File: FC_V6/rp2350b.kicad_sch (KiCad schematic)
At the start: 44 parts, among them J1 USB_C_Receptacle_USB2.0_16P, J2 Conn_ARM_JTAG_SWD_10, SW1 KMR2, SW2 KMR2, U1 RP2350B, U2 W25Q128JV, Y1 ABM8-272-T3

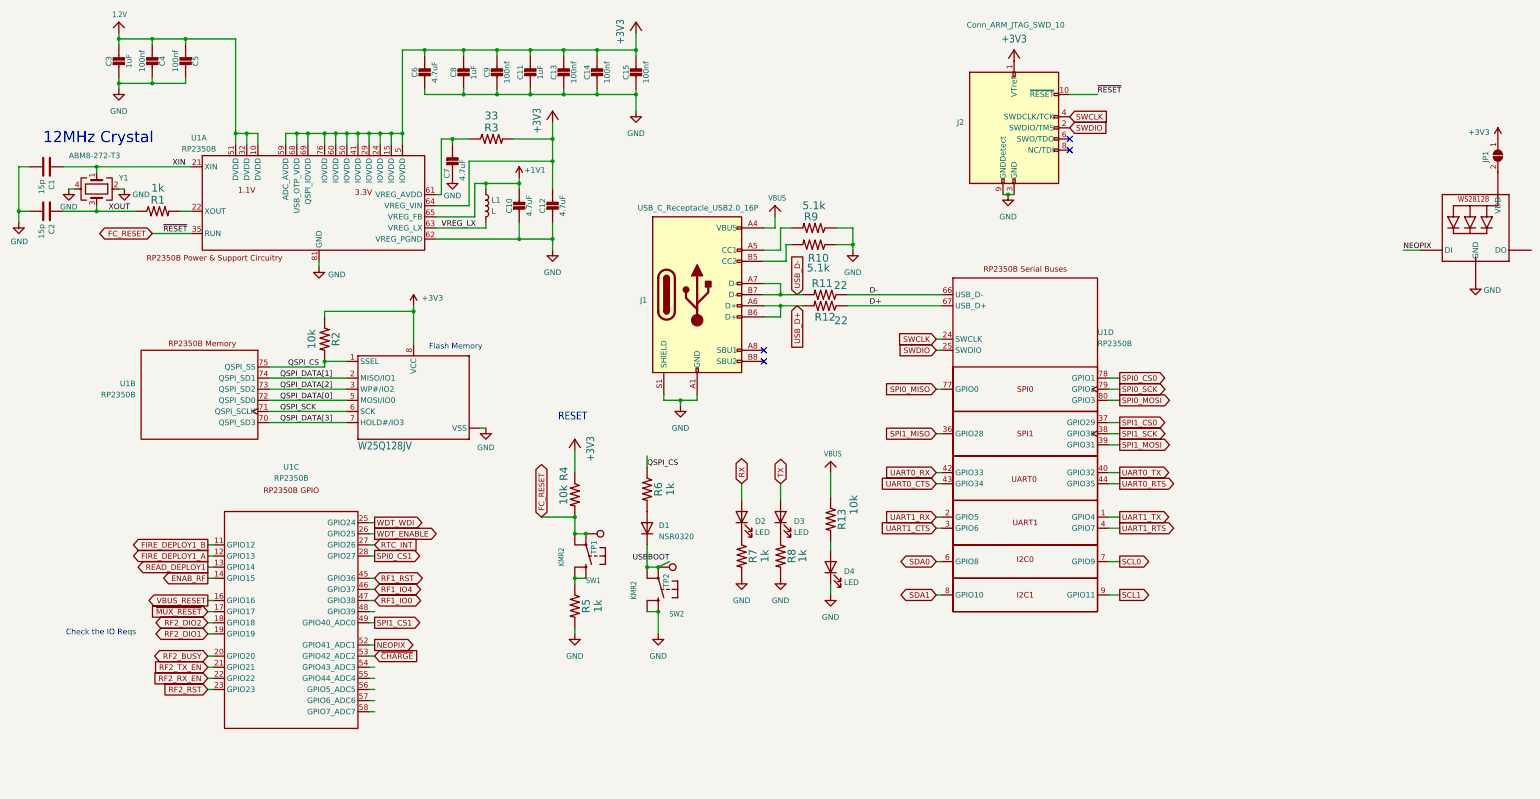
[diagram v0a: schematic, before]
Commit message: Updated Flash Memory Schematic
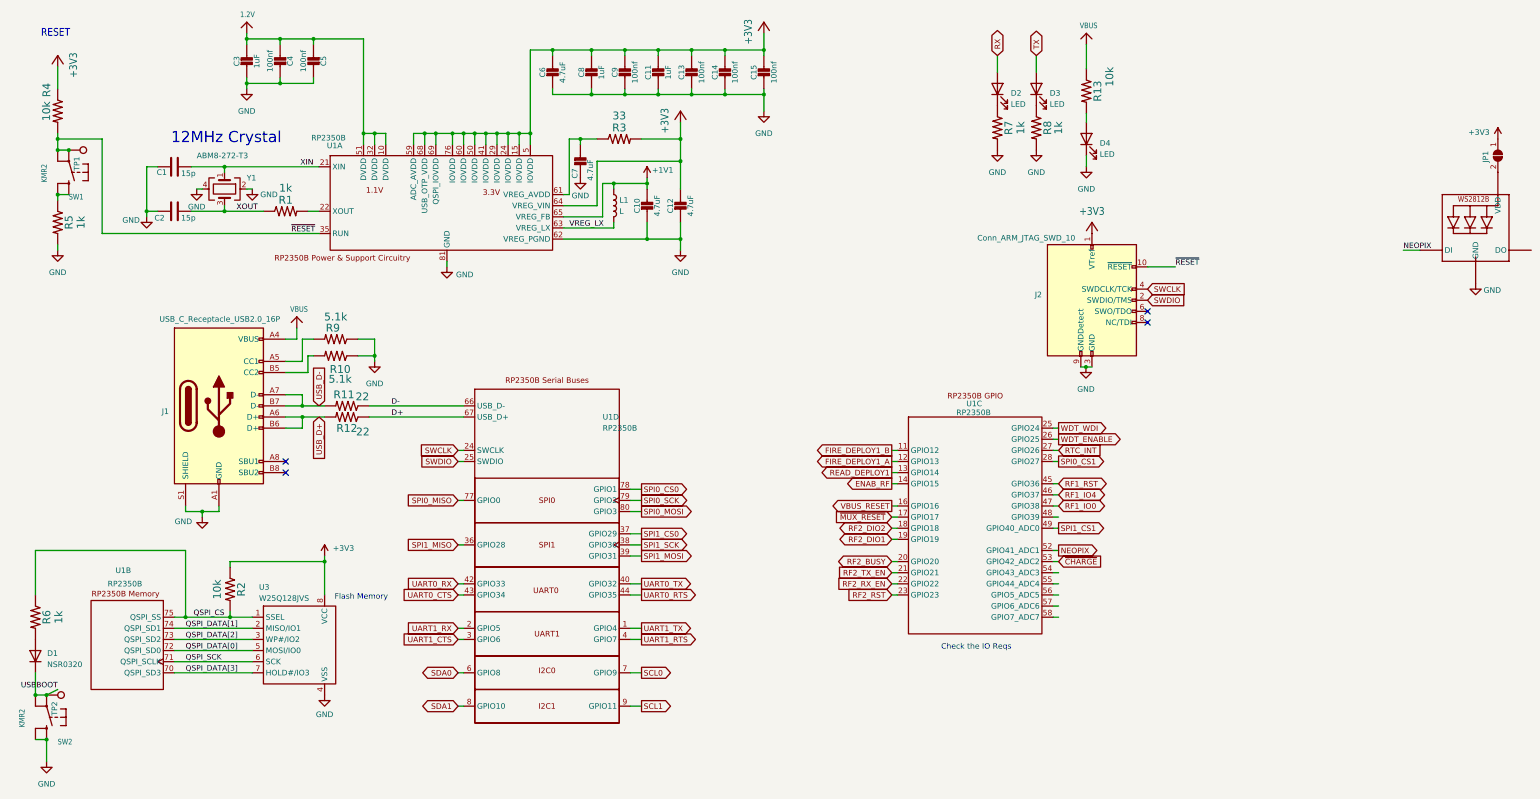
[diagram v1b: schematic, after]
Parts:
- removed U2: W25Q128JV, Package_SO:SOIC-8_5.275x5.275mm_P1.27mm, symbol Adafruit ItsyBitsy RP2040-eagle-import:SPIFLASH_8PIN_4X4
- added U3: W25Q128JVS, Package_SO:SOIC-8_5.3x5.3mm_P1.27mm, symbol PROVES:W25Q128JV
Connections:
- net +3V3: now also U3.8 (VCC)
- net GND: now also U3.4 (VSS)
- net QSPI_CS: now also U3.1 (SSEL)
- net QSPI_DATA[0]: now also U3.5 (MOSI/IO0)
- net QSPI_DATA[1]: now also U3.2 (MISO/IO1)
- net QSPI_DATA[2]: now also U3.3 (WP#/IO2)
- net QSPI_DATA[3]: now also U3.7 (HOLD#/IO3)
- net QSPI_SCK: now also U3.6 (SCK)
- net FC_RESET renamed ~{RESET}
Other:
- moved on the sheet: C1, C10, C11, C12, C13, C14, C15, C2, C3, C4, C5, C6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

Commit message: Updated LSM6DSOX Symbol
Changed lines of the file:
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@@
 		(on_board yes)
 		(dnp no)
-		(fields_autoplaced yes)
 		(property "Reference" "U1"
-			(at 149.86 109.2171 0)
+			(at 152.146 98.298 0)
 			(effects
 				(font
@@
 		)
 		(property "Value" "RP2350B"
-			(at 149.86 111.7571 0)
+			(at 152.146 100.838 0)
 			(effects
 				(font

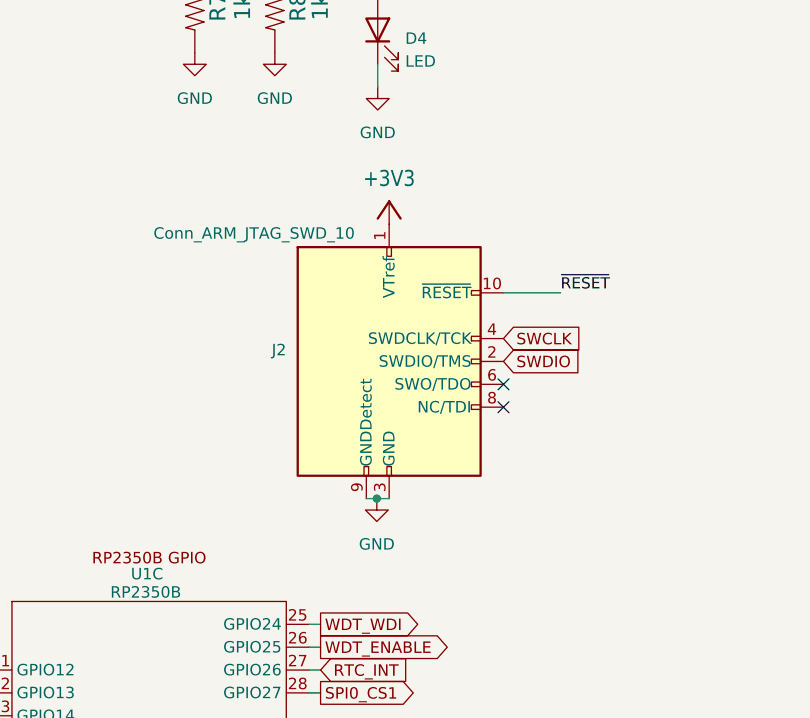
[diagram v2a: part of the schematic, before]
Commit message: Added 3v3 Load Switch Schematic
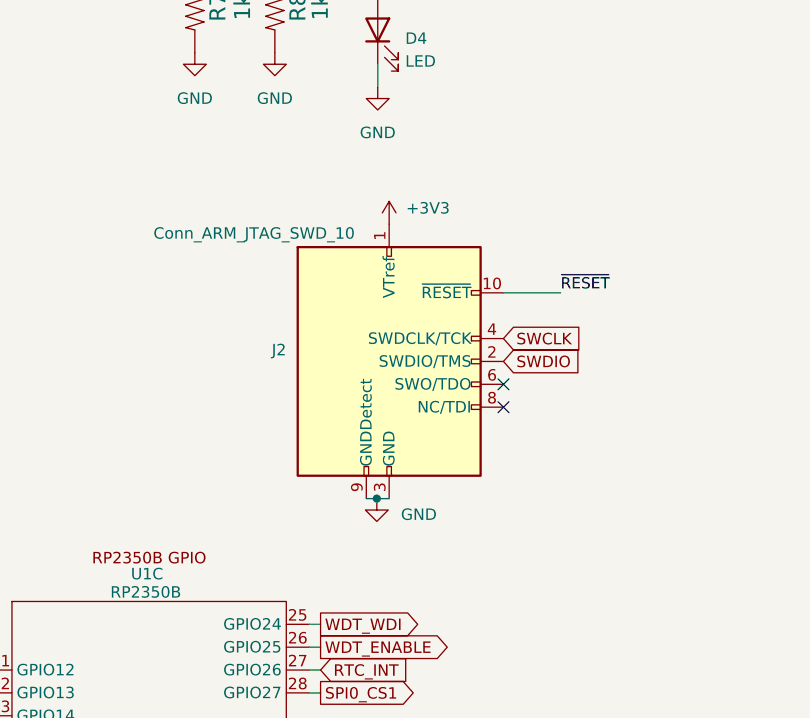
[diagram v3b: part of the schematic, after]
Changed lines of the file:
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@@
-	)
-	(symbol
-		(lib_id "Adafruit ItsyBitsy RP2040-eagle-import:+3V3")
-		(at 261.62 64.77 0)
-		(unit 1)
-		(exclude_from_sim no)
-		(in_bom yes)
-		(on_board yes)
-		(dnp no)
-		(fields_autoplaced yes)
-		(property "Reference" "#+3V04"
-			(at 261.62 64.77 0)
-			(effects
-				(font
-					(size 1.27 1.27)
-				)
-				(hide yes)
-			)
-		)
-		(property "Value" "+3V3"
-			(at 261.62 62.23 0)
-			(effects
-				(font
-					(size 1.778 1.5113)
-				)
-			)
-		)
-		(property "Footprint" "Adafruit ItsyBitsy RP2040:"
-			(at 261.62 64.77 0)
-			(effects
-				(font
-					(size 1.27 1.27)
-				)
-				(hide yes)
-			)
-		)
-		(property "Datasheet" ""
-			(at 261.62 64.77 0)
-			(effects
-				(font
-					(size 1.27 1.27)
-				)
-				(hide yes)
-			)
-		)
-		(property "Description" ""
-			(at 261.62 64.77 0)
-			(effects
-				(font
-					(size 1.27 1.27)
-				)
-				(hide yes)
-			)
-		)
-		(pin "1"
-		)
-		(instances
-			(project "FC_V6"
-				(path "/f080da98-69f4-43da-b75c-192226370aa3/62153ef6-d39c-4c3d-8add-145da0e06ff3"
-					(reference "#+3V04")
-					(unit 1)
-				)
-			)
-		)
 	)
 	(symbol
@@
 	)
 	(symbol
+		(lib_name "+3V3_2")
+		(lib_id "power:+3V3")
+		(at 261.62 67.31 0)
+		(unit 1)
+		(exclude_from_sim no)
+		(in_bom yes)
+		(on_board yes)
+		(dnp no)
+		(property "Reference" "#PWR029"
+			(at 261.62 71.12 0)
+			(effects
+				(font
+					(size 1.27 1.27)
+				)
+				(hide yes)
+			)
+		)
+		(property "Value" "+3V3"
+			(at 265.938 65.532 0)
+			(effects
+				(font
+					(size 1.27 1.27)
+				)
+			)
+		)
+		(property "Footprint" ""
+			(at 261.62 67.31 0)
+			(effects
+				(font
+					(size 1.27 1.27)
+				)
+				(hide yes)
+			)
+		)
+		(property "Datasheet" ""
+			(at 261.62 67.31 0)
+			(effects
+				(font
+					(size 1.27 1.27)
+				)
+				(hide yes)
+			)
+		)
+		(property "Description" ""
+			(at 261.62 67.31 0)
+			(effects
+				(font
+					(size 1.27 1.27)
+				)
+				(hide yes)
+			)
+		)
+		(pin "1"
+		)
+		(instances
+			(project "FC_V6"
+				(path "/f080da98-69f4-43da-b75c-192226370aa3/62153ef6-d39c-4c3d-8add-145da0e06ff3"
+					(reference "#PWR029")
+					(unit 1)
+				)
+			)
+		)
+	)
+	(symbol
 		(lib_name "GND_8")
 		(lib_id "power:GND")
@@
 		(on_board yes)
 		(dnp no)
-		(fields_autoplaced yes)
 		(property "Reference" "#PWR019"
 			(at 260.2484 104.14 0)
@@
 		)
 		(property "Value" "GND"
-			(at 260.2484 102.87 0)
-			(effects
-				(font
+			(at 264.922 99.568 0)
+			(effects
+				(font
